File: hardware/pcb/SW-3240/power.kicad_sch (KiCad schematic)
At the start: 36 parts, among them J12 PWR, J13 BAT, SW5 PWR_SW, U8 TPS5430DDA, U9 LM2576S-5

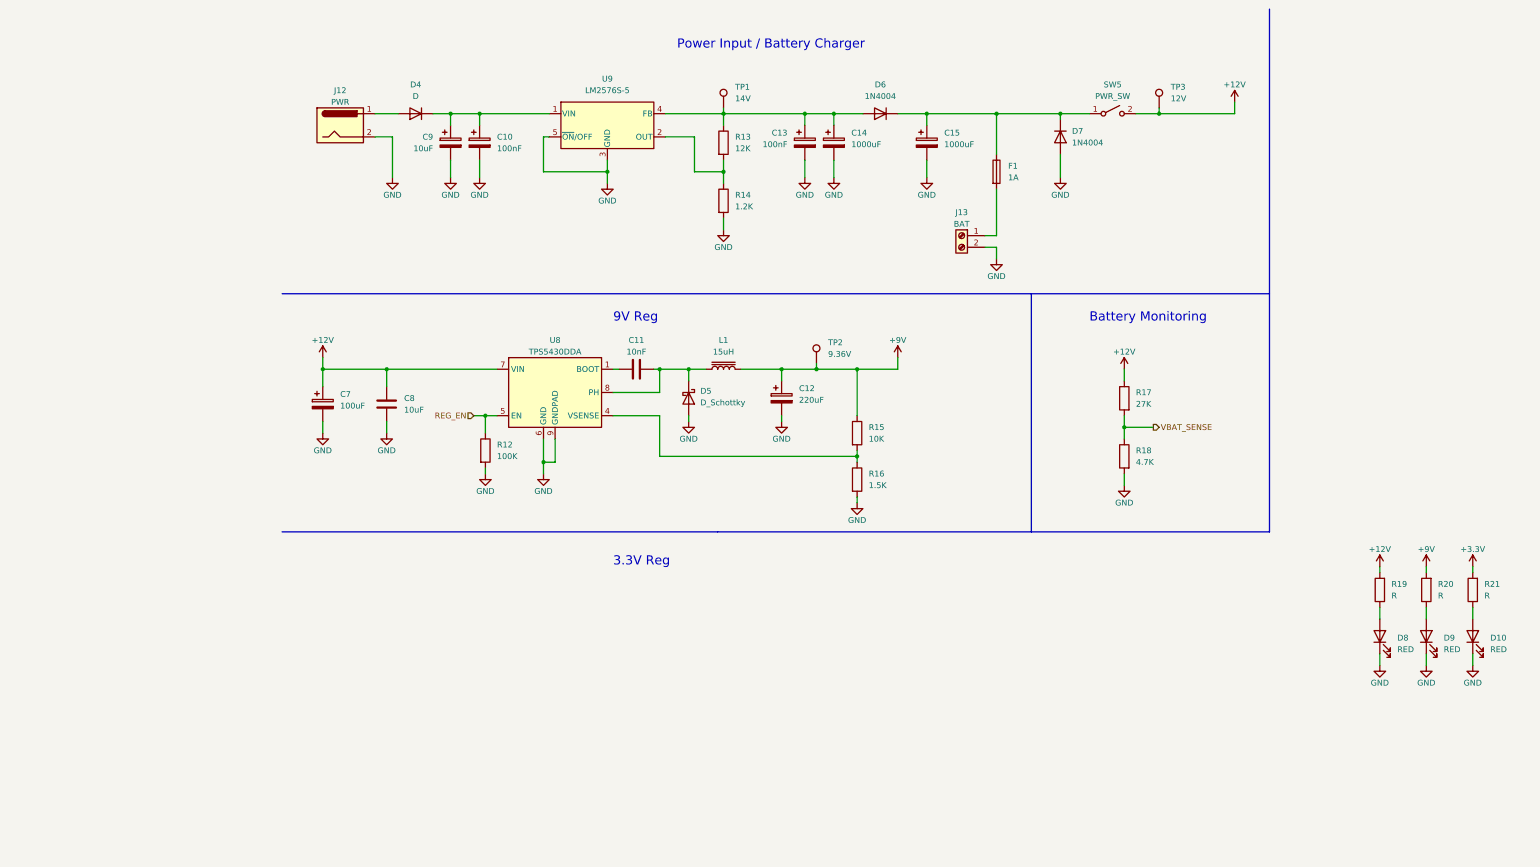
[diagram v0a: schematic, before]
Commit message: split dual esp32 modules
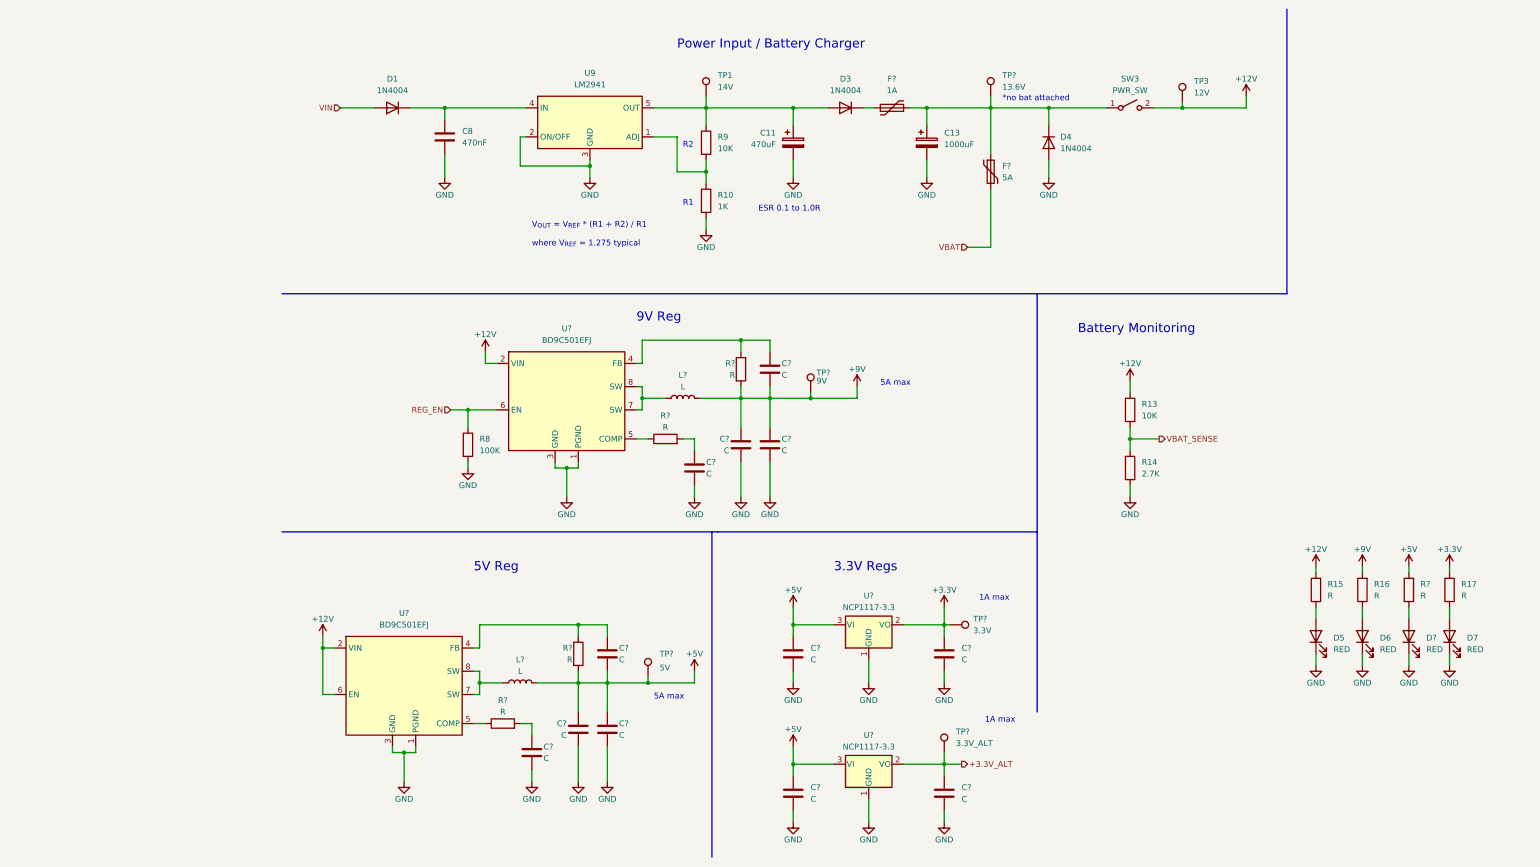
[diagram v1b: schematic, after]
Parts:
- removed C11: 10nF, Capacitor_SMD:C_0603_1608Metric, symbol Device:C
- removed C12: 220uF, Capacitor_SMD:C_0603_1608Metric, symbol Device:C_Polarized
- removed C14: 1000uF, Capacitor_THT:CP_Radial_D8.0mm_P5.00mm, symbol Device:C_Polarized
- removed C7: 100uF, Capacitor_SMD:C_0603_1608Metric, symbol Device:C_Polarized
- removed C8: 10uF, Capacitor_SMD:C_0603_1608Metric, symbol Device:C
- removed C9: 10uF, Capacitor_SMD:C_0603_1608Metric, symbol Device:C_Polarized
- removed D5: D_Schottky, symbol Device:D_Schottky
- removed F1: 1A, symbol Device:Fuse
- removed J12: PWR, SaawLib:BarrelJack_CUI_PJ-102AH_Horizontal, symbol Connector:Barrel_Jack
- removed J13: BAT, Connector_JST:JST_XH_B2B-XH-A_1x02_P2.50mm_Vertical, symbol Connector:Screw_Terminal_01x02
- removed L1: 15uH, symbol Device:L_Iron
- removed R15: 10K, Resistor_SMD:R_0603_1608Metric, symbol Device:R
- removed R16: 1.5K, Resistor_SMD:R_0603_1608Metric, symbol Device:R
- removed TP2: 9.36V, TestPoint:TestPoint_THTPad_D2.0mm_Drill1.0mm, symbol Connector:TestPoint
- removed U8: TPS5430DDA, Package_SO:TI_SO-PowerPAD-8_ThermalVias, symbol Regulator_Switching:TPS5430DDA
- added C? (x8): C, symbol Device:C
- added C? (x4): C, Capacitor_SMD:C_0603_1608Metric, symbol Device:C
- added D?: RED, LED_SMD:LED_0805_2012Metric, symbol Device:LED
- added F?: 5A, symbol Device:Polyfuse
- added F?: 1A, symbol Device:Polyfuse
- added L? (x2): L, symbol Device:L
- added R? (x4): R, symbol Device:R
- added R?: R, Resistor_SMD:R_0603_1608Metric, symbol Device:R
- added TP?: 3.3V_ALT, TestPoint:TestPoint_THTPad_D2.0mm_Drill1.0mm, symbol Connector:TestPoint
- added TP?: 13.6V, TestPoint:TestPoint_THTPad_D2.0mm_Drill1.0mm, symbol Connector:TestPoint
- added TP?: 5V, TestPoint:TestPoint_THTPad_D2.0mm_Drill1.0mm, symbol Connector:TestPoint
- added TP?: 3.3V, TestPoint:TestPoint_THTPad_D2.0mm_Drill1.0mm, symbol Connector:TestPoint
- added TP?: 9V, TestPoint:TestPoint_THTPad_D2.0mm_Drill1.0mm, symbol Connector:TestPoint
- added U? (x2): NCP1117-3.3, Package_TO_SOT_SMD:SOT-223-3_TabPin2, symbol Regulator_Linear:NCP1117-3.3_SOT223
- added U? (x2): BD9C501EFJ, symbol SaawLib:BD9C501EFJ
- C11: renamed from C13; value 100nF -> 470uF
- C8: renamed from C10; value 100nF -> 470nF; symbol Device:C_Polarized -> Device:C
- D1: renamed from D4; value D -> 1N4004
- R10: renamed from R14; value 1.2K -> 1K
- R13: renamed from R17; value 27K -> 10K
- R14: renamed from R18; value 4.7K -> 2.7K
- R9: renamed from R13; value 12K -> 10K
- U9: value LM2576S-5 -> LM2941; symbol Regulator_Switching:LM2576S-5 -> SaawLib:LM2941
- renumbered C15 to C13, D6 to D3, D7 to D4, D8 to D5, D9 to D6, D10 to D7, R19 to R15, R20 to R16, R21 to R17, R12 to R8, SW5 to SW3
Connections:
- net +12V: now also U?.2 (VIN), U?.2 (VIN), U?.6 (EN)
- net +3V3: now also C?.1, TP?.1, U?.2 (VO)
- net +9V: now also C?.1, C?.1, C?.2, L?.2, R?.2, TP?.1
- net GND: now also U9.2 (ON/OFF), C?.2, C?.2, C?.2, C?.2, C?.2, C?.2, C?.2, C?.2, C?.2, C?.2, D?.1 (K), U?.1 (GND), U?.1 (GND), U?.1 (PGND), U?.1 (PGND), U?.3 (GND), U?.3 (GND); no longer U9.5 (~{ON}/OFF)
- net REG_EN: now also U?.6 (EN)
- net at C13.1, D4.1 (K), SW3.1 (A): now also F?.1, F?.2, TP?.1; no longer D3.1 (K)
- net at C11.1, D3.2 (A), R9.1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: now also U9.5 (OUT); no longer U9.4 (FB)
- net at R10.1, R9.2: now also U9.1 (ADJ); no longer U9.2 (OUT)
- net at C8.1, D1.1 (K): now also U9.4 (IN); no longer U9.1 (VIN)
- net VIN: now reaches D1.2 (A)
- new net: C?.1, R?.1, U?.4 (FB) (x2)
- new net: D?.2 (A), R?.1
- new net: C?.1, R?.2 (x2)
- new net: R?.1, U?.5 (COMP) (x2)
- new net: L?.1, U?.7 (SW), U?.8 (SW) (x2)
- new net: D3.1 (K), F?.1
- new net +3.3V_ALT: C?.1, TP?.1, U?.2 (VO)
- new net +5V: C?.1, C?.1, C?.1, C?.1, C?.2, L?.2, R?.2, R?.2, TP?.1, U?.3 (VI), U?.3 (VI)
- new net VBAT: F?.2
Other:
- note added: "*no bat attached"
- note added: "1A max"
- note added: "3.3V Regs"
- note added: "5A max"
- note added: "5V Reg"
- note added: "ESR 0.1 to 1.0R"
- note added: "R1"
- note added: "R2"
- note added: "V_{OUT} = V_{REF} * (R1 + R2) / R1 where V_{REF} = 1.275 typical"
- note removed: "3.3V Reg"
- company: (none) -> saawsm
- moved on the sheet: C11, D1, D3, D4, D5, D6, D7, R10, R13, R14, R15, R16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

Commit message: fix footprint pin mismatch
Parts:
- removed C? (x8): C, symbol Device:C
- removed C?: C, Capacitor_SMD:C_0603_1608Metric, symbol Device:C
- removed L?: L, symbol Device:L
- removed R? (x4): R, symbol Device:R
- removed TP?: 5V, TestPoint:TestPoint_THTPad_D2.0mm_Drill1.0mm, symbol Connector:TestPoint
- removed TP?: 9V, TestPoint:TestPoint_THTPad_D2.0mm_Drill1.0mm, symbol Connector:TestPoint
- removed U? (x2): BD9C501EFJ, symbol SaawLib:BD9C501EFJ
- added C10: 1000uF, Capacitor_SMD:C_0603_1608Metric, symbol Device:C_Polarized
- added C11: 100nF, symbol Device:C
- added C13: C, symbol Device:C_Polarized
- added C17, C6: 10uF, Capacitor_SMD:C_0603_1608Metric, symbol Device:C
- added C19, C20: 100nF, Capacitor_SMD:C_0603_1608Metric, symbol Device:C
- added C5, C7: 100uF, Capacitor_SMD:C_0603_1608Metric, symbol Device:C_Polarized
- added C9: 22nF, symbol Device:C
- added D2: 1N5822, symbol Device:D_Schottky
- added D3: D_Schottky, symbol Device:D_Schottky
- added L2: 8.2uH, symbol Device:L_Ferrite
- added R14: 100K, symbol Device:R
- added R15: 9K, symbol Device:R
- added R9: 84.5K, Resistor_SMD:R_0603_1608Metric, symbol Device:R
- added TP1: EN, TestPoint:TestPoint_THTPad_D2.0mm_Drill1.0mm, symbol Connector:TestPoint
- added TP2: 5V, TestPoint:TestPoint_THTPad_D2.0mm_Drill1.0mm, symbol Connector:TestPoint
- added TP4: 9V, TestPoint:TestPoint_THTPad_D2.0mm_Drill1.0mm, symbol Connector:TestPoint
- added U10: LMR14050, symbol SaawLib:LMR14050
- added U8: LM2576-5, Package_TO_SOT_SMD:TO-263-5_TabPin3, symbol Regulator_Switching:LM2576S-5
- C12: renamed from C11; value 470uF -> 1000uF
- C15, C16, C18: renamed from C?; value C -> 10uF
- L1: renamed from L?; value L -> 100uH
- TP5: renamed from TP?; value 13.6V -> 13.5V
- gave numbers to parts that had none: 8
- renumbered C13 to C14, D5 to D4, D3 to D5, D7 to D8, D4 to D9, R9 to R10, R10 to R11, R15 to R12, R16 to R13, R13 to R18, R14 to R19, TP1 to TP3, TP3 to TP6
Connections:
- net +12V: now also C5.1, C6.1, C7.1, U10.2 (VIN), U8.1 (VIN)
- net +3.3V_ALT: now also C20.1
- net +3V3: now also C17.1, C19.1
- net +5V: now also L1.2, C10.1, TP2.1, U8.4 (FB)
- net +9V: now also C13.1, L2.2, R14.1, TP4.1; no longer L1.2
- net GND: now also C10.2, C13.2, C17.2, C19.2, C20.2, C5.2, C6.2, C7.2, C9.1, D2.2 (A), D3.2 (A), R15.2, R9.2, U10.7 (GND), U10.9 (GNDPAD), U8.3 (GND), U8.5 (~{ON}/OFF)
- net REG_EN: now also TP1.1, U10.3 (EN)
- net at L1.1: now also D2.1 (K), U8.2 (OUT)
- new net: R14.2, R15.1, U10.5 (FB)
- new net: C9.2, U10.6 (SS)
- new net: C11.1, U10.1 (BOOT)
- new net: C11.2, D3.1 (K), L2.1, U10.8 (SW)
- new net: R9.1, U10.4 (RT/SYNC)
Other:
- note added: "3A max"
- note added: "7A RMS/10A saturation"
- note added: "Status LEDs"
- note added: "V_{IN_MAX} = 20V V_{OUT} = 9V I_{OUT} = 5A f_{SW} = 300 kHz K_{IND} = 0.4 t_{ss} = 5ms"
- note removed: "*no bat attached"
- moved on the sheet: C15, C16, C18, D4, D6, D7, D8, L1, R12, R13, R16, R17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

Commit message: many changes
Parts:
- removed C10: 1000uF, Capacitor_SMD:C_0603_1608Metric, symbol Device:C_Polarized
- removed C13: C, symbol Device:C_Polarized
- removed C5, C7: 100uF, Capacitor_SMD:C_0603_1608Metric, symbol Device:C_Polarized
- removed D4, D7: RED, LED_SMD:LED_0805_2012Metric, symbol Device:LED
- removed L1: 100uH, symbol Device:L
- removed TP2: 5V, TestPoint:TestPoint_THTPad_D2.0mm_Drill1.0mm, symbol Connector:TestPoint
- removed U8: LM2576-5, Package_TO_SOT_SMD:TO-263-5_TabPin3, symbol Regulator_Switching:LM2576S-5
- added C11: 15nF, Capacitor_SMD:C_0603_1608Metric, symbol Device:C
- added C12: 100nF, Capacitor_SMD:C_0603_1608Metric, symbol Device:C
- added C14: 1nF, Capacitor_SMD:C_0603_1608Metric, symbol Device:C
- added C15: 10pF, Capacitor_SMD:C_0603_1608Metric, symbol Device:C
- added C16, C18, C19: 22uF/16V/X7R, Capacitor_SMD:C_1210_3225Metric, symbol Device:C
- added C21: 330pF, Capacitor_SMD:C_0603_1608Metric, symbol Device:C
- added C23, C24: 47uF, Capacitor_SMD:CP_Elec_5x4.4, symbol Device:C_Polarized
- added C8, C9: 10uF/50V/X7R, Capacitor_SMD:C_1210_3225Metric, symbol Device:C
- added L1: 12uH, symbol Device:L_Ferrite
- added R15: 10.2K, Resistor_SMD:R_0603_1608Metric, symbol Device:R
- added R8: 169K, Resistor_SMD:R_0603_1608Metric, symbol Device:R
- added R9: 39.2K, Resistor_SMD:R_0603_1608Metric, symbol Device:R
- added TP3: 5V, TestPoint:TestPoint_THTPad_D2.0mm_Drill1.0mm, symbol Connector:TestPoint
- added U8: TPS54231, Package_SO:SOIC-8_3.9x4.9mm_P1.27mm, symbol SaawLib:TPS54231
- C13: renamed from C9; footprint (none) -> Capacitor_SMD:C_0603_1608Metric
- C17: renamed from C11; footprint (none) -> Capacitor_SMD:C_0603_1608Metric
- C20: renamed from C12; value 1000uF -> 470uF; footprint Capacitor_SMD:C_0603_1608Metric -> Capacitor_THT:C_Radial_D8.0mm_H11.5mm_P3.50mm
- C22: renamed from C14; value 1000uF -> 470uF; footprint Capacitor_THT:CP_Radial_D8.0mm_P5.00mm -> Capacitor_THT:C_Radial_D8.0mm_H11.5mm_P3.50mm
- C7: renamed from C6; value 10uF -> 10uF/50V/X7R; footprint Capacitor_SMD:C_0603_1608Metric -> Capacitor_SMD:C_1210_3225Metric
- D1: value 1N4004 -> SS34; footprint Diode_SMD:D_SOD-123F -> Diode_SMD:D_SMC
- D2: value 1N5822 -> SSA24; footprint (none) -> Diode_SMD:D_SMA; MPN (none) -> SSA24
- D3: value D_Schottky -> B530C-13-F; MPN (none) -> B530C-13-F
- D4: renamed from D5; value 1N4004 -> SS34; footprint Diode_SMD:D_SOD-123F -> Diode_SMD:D_SMC
- D7: renamed from D9; value 1N4004 -> S5DC-13-F; footprint Diode_SMD:D_SOD-123F -> Diode_SMD:D_SMC
- L2: value 8.2uH -> 1.5uH; MPN (none) -> SRN8040-1R5Y
- R11: renamed from R9; value 84.5K -> 13.7K
- R12: value R -> 26.7K
- R16: value R -> 1.96K
- R17: renamed from R14; value 100K -> 110K; footprint (none) -> Resistor_SMD:R_0603_1608Metric
- R18: renamed from R15; value 9K -> 10K; footprint (none) -> Resistor_SMD:R_0603_1608Metric
- R19: renamed from R13; value R -> 1K
- R20: renamed from R17; value R -> 470
- U10: footprint (none) -> Package_SO:TI_SO-PowerPAD-8
- renumbered C8 to C10, C15 to C25, C16 to C26, C17 to C27, C18 to C28, C19 to C29, C20 to C30, D6 to D5, D8 to D6, R8 to R10, R10 to R13, R11 to R14, R18 to R21, R19 to R22, SW3 to SW1, TP3 to TP2
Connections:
- net +12V: now also C8.2, C9.2, R8.2, U8.2 (VIN); no longer R12.2
- net +5V: now also C16.2, C18.2, C19.2, L1.2, R15.2, TP3.1; no longer R16.2
- net +9V: now also C21.2, C23.1, C24.1
- net GND: now also R16.1, C11.1, C14.1, C15.1, C16.1, C18.1, C19.1, C23.2, C24.2, C8.1, C9.1, R9.1, U8.7 (GND)
- net at R17.2, R18.1, U10.5 (FB): now also C21.1
- net at R12.1: now also C14.2
- net at D2.1 (K): now also C12.2, L1.1, U8.8 (PH)
- new net: R15.1, R16.2, U8.5 (VSENSE)
- new net: C11.2, U8.4 (SS)
- new net: R8.1, R9.2, U8.3 (EN)
- new net: C12.1, U8.1 (BOOT)
- new net: C15.2, R12.2, U8.6 (COMP)
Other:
- note added: "2A max"
- note added: "V_{IN_MAX} = 11-16V V_{OUT} = 5V I_{OUT} = 2A f_{SW} = 570 kHz UVLO_{START} = 10.5V UVLO_{hy} = 0.5V"
- note added: "V_{IN} = 11 - 16V V_{OUT} = 9V I_{OUT} = 5A f_{SW} = 1.699 MHz t_{ss} = 5ms"
- note added: "V_{OUT} = 1.275V * (R1 + R2) / R1"
- note added: "~1A max"
- note removed: "1A max"
- note removed: "3A max"
- note removed: "7A RMS/10A saturation"
- note removed: "V_{IN_MAX} = 20V V_{OUT} = 9V I_{OUT} = 5A f_{SW} = 300 kHz K_{IND} = 0.4 t_{ss} = 5ms"
- note removed: "V_{OUT} = V_{REF} * (R1 + R2) / R1 where V_{REF} = 1.275 typical"
- moved on the sheet: C13, C17, C7, D3, D5, D6, L2, R10, R11, R17, R18, R19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

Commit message: use 5v for front panel connector
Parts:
- removed C26, C28: 10uF, Capacitor_SMD:C_0603_1608Metric, symbol Device:C
- removed C30: 100nF, Capacitor_SMD:C_0603_1608Metric, symbol Device:C
- removed D5, D6: RED, LED_SMD:LED_0805_2012Metric, symbol Device:LED
- removed R19: 1K, Resistor_SMD:R_0603_1608Metric, symbol Device:R
- removed R20: 470, Resistor_SMD:R_0603_1608Metric, symbol Device:R
- removed TP8: 3.3V_ALT, TestPoint:TestPoint_THTPad_D2.0mm_Drill1.0mm, symbol Connector:TestPoint
- removed U12: NCP1117-3.3, Package_TO_SOT_SMD:SOT-223-3_TabPin2, symbol Regulator_Linear:NCP1117-3.3_SOT223
- added D? (x2): RED, LED_SMD:LED_0805_2012Metric, symbol Device:LED
- added R?: 470, Resistor_SMD:R_0603_1608Metric, symbol Device:R
- added R?: 1K, Resistor_SMD:R_0603_1608Metric, symbol Device:R
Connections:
- net +3V3: now also R?.2
- net +9V: now also R?.2
- net GND: now also D?.1 (K), D?.1 (K)
- new net: D?.2 (A), R?.1 (x2)
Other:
- note added: "14V min"
- note added: "22V min"
- note added: "3.3V Reg"
- note added: "C: 10-47uF ESR: 0.1R max Irms: 1.1A min VDC: 22V min"
- note added: "C: 2.2-100uF ESR: 0.08R max Irms: 2.7A min VDC: 20V min"
- note added: "C: 35-106uF ESR: 0.02R max Irms: 490mA min VDC: 12V min"
- note added: "C: 37-93uF ESR: 0.015R max Irms: 146mA min VDC: 8V min"
- note added: "L: 1.1-5.8uH DCR: 0.02R max IDC: 6.7A min"
- note added: "L: 11-16uH DCR: 0.1R max IDC: 3A min"
- note added: "VRRM: 23V min Io: 1.8A min Vf: ~0.5V"
- note added: "VRRM: 26V min Io: 5A min Vf: ~0.5V"
- note removed: "3.3V Regs"
- moved on the sheet: C14, C15, C16, C18, C19, C25, C27, C29, L1, R12, R15, R16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
